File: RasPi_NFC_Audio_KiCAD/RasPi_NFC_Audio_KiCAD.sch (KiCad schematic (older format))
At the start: 19 parts, among them J1 Barrel_Jack_Switch, J2 Conn_02x20_Odd_Even, J3 Connector_01x10, U1 MIC5225-3.3V

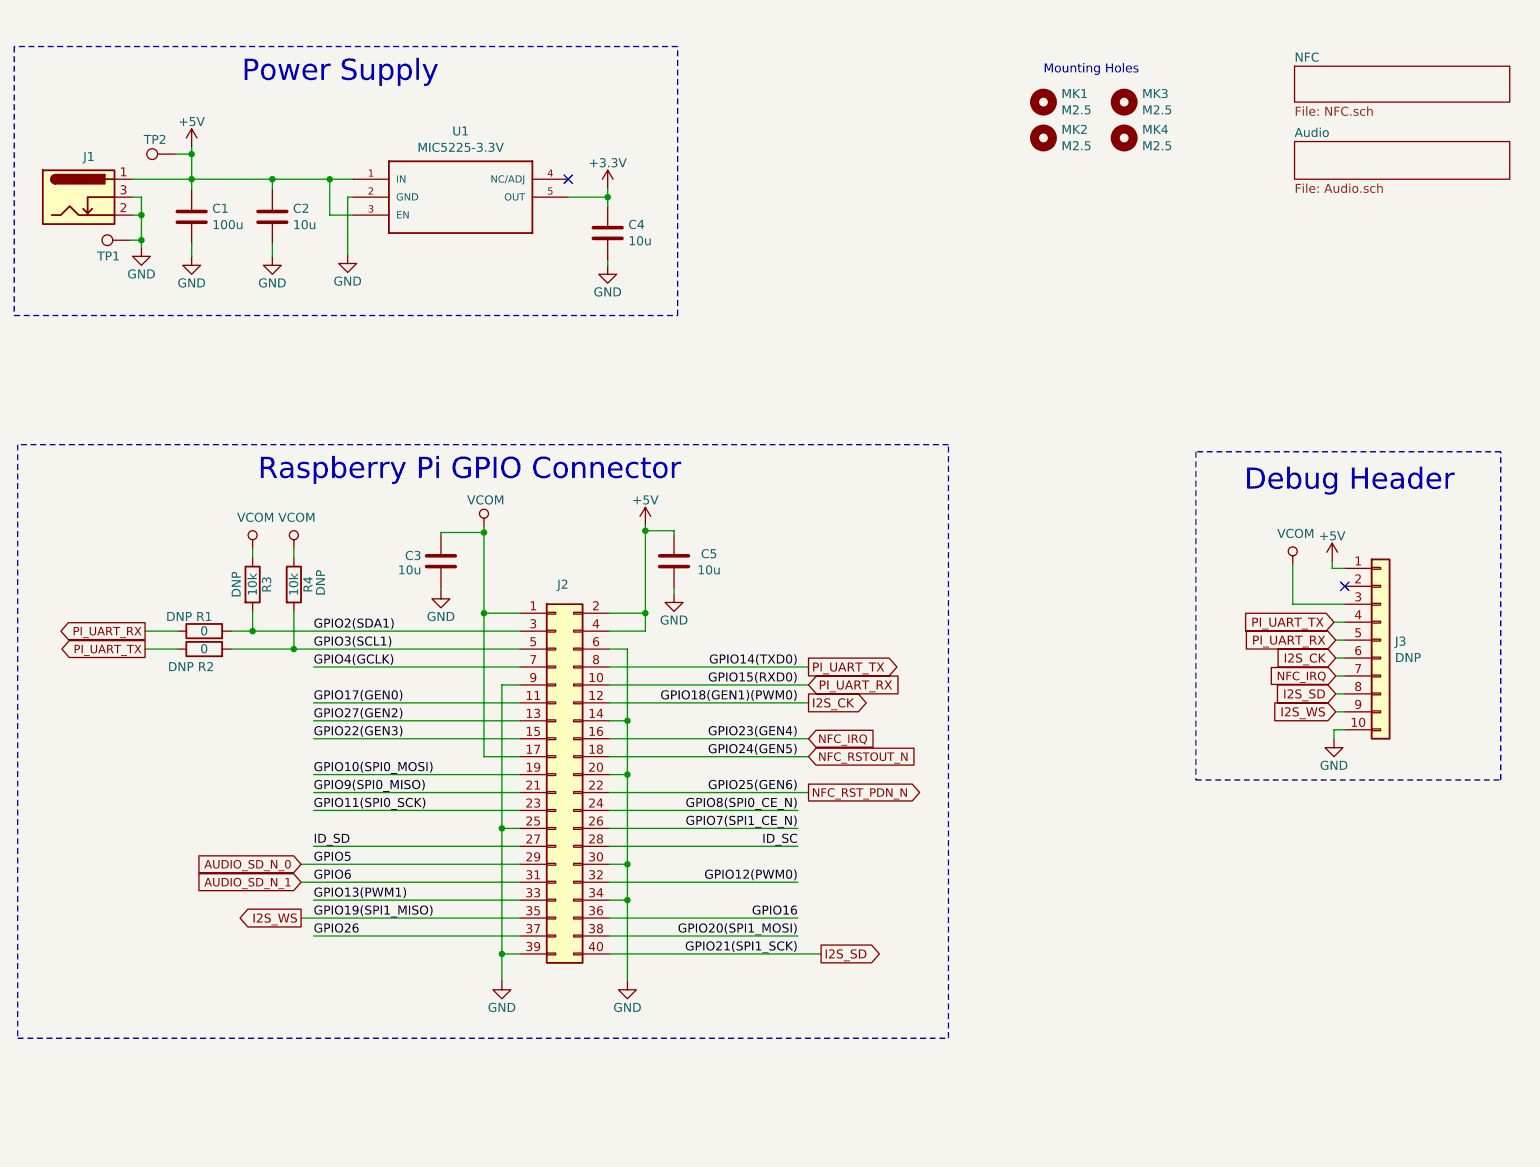
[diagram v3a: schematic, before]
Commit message: Schematic updates
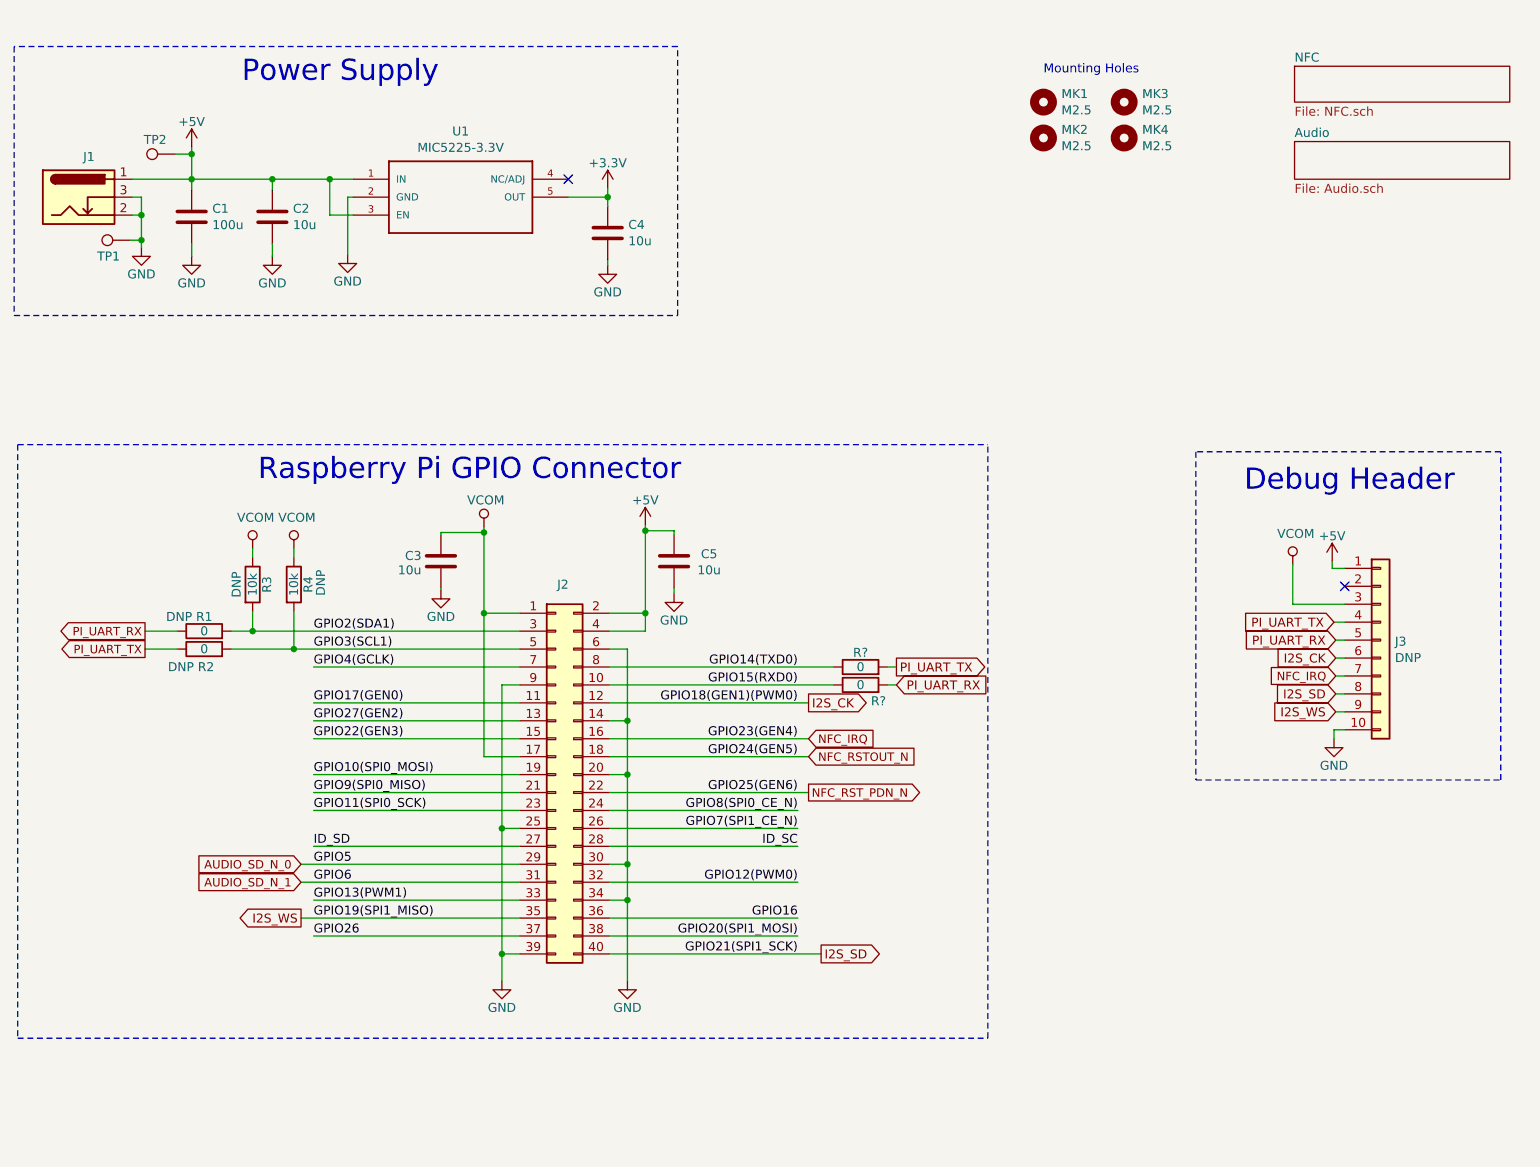
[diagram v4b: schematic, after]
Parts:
- added R? (x2): 0, Resistors_SMD:R_0603_HandSoldering, symbol Device:R
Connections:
- net PI_UART_RX: now also R?.2; no longer J2.10 (Pin_10)
- net PI_UART_TX: now also R?.2; no longer J2.8 (Pin_8)
- new net GPIO14(TXD0): J2.8 (Pin_8), R?.1
- new net GPIO15(RXD0): J2.10 (Pin_10), R?.1
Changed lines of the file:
@@
 EESchema Schematic File Version 4
 LIBS:RasPi_NFC_Audio_KiCAD-cache
-EELAYER 29 0
+EELAYER 30 0
 EELAYER END
 $Descr A4 11693 8268
@@
 Text GLabel 2670 6190 0    50   Output ~ 0
 I2S_WS
-Text GLabel 5500 4790 2    50   Output ~ 0
+Text GLabel 5990 4790 2    50   Output ~ 0
 PI_UART_TX
-Text GLabel 5500 4890 2    50   Input ~ 0
+Text GLabel 5990 4890 2    50   Input ~ 0
 PI_UART_RX
 Wire Wire Line
-	4390 4890 5500 4890
-Wire Wire Line
-	4390 4790 5500 4790
+	4390 4890 5640 4890
+Wire Wire Line
+	4390 4790 5640 4790
 $Comp
 L power:GND #PWR0101
@@
 	1090 3550 1090 6860
 Wire Notes Line
-	1090 6860 6280 6860
-Wire Notes Line
-	6280 6860 6280 3550
-Wire Notes Line
-	6280 3550 1090 3550
+	6500 6860 6500 3550
 Text Notes 2430 3760 0    118  ~ 0
 Raspberry Pi GPIO Connector
@@
 Wire Wire Line
 	1730 2170 1780 2170
+$Comp
+L Device:R R?
+U 1 1 5E234EC3
+P 5790 4790
+AR Path="/5E17696B/5E234EC3" Ref="R?"  Part="1"
+AR Path="/5E234EC3" Ref="R?"  Part="1"
+F 0 "R?" V 5870 4790 50  0000 C CNN
+F 1 "0" V 5790 4790 50  0000 C CNN
+F 2 "Resistors_SMD:R_0603_HandSoldering" V 5720 4790 50  0001 C CNN
+F 3 "" H 5790 4790 50  0001 C CNN
+F 4 "RC0603JR-070RL" H 5790 4790 50  0001 C CNN "Part #"
+F 5 "311-0.0GRCT-ND" H 5790 4790 50  0001 C CNN "DigiKey"
+	1    5790 4790
+	0    -1   -1   0
+$EndComp
+$Comp
+L Device:R R?
+U 1 1 5E23DE1B
+P 5790 4890
+AR Path="/5E17696B/5E23DE1B" Ref="R?"  Part="1"
+AR Path="/5E23DE1B" Ref="R?"  Part="1"
+F 0 "R?" V 5700 4790 50  0000 C CNN
+F 1 "0" V 5790 4890 50  0000 C CNN
+F 2 "Resistors_SMD:R_0603_HandSoldering" V 5720 4890 50  0001 C CNN
+F 3 "" H 5790 4890 50  0001 C CNN
+F 4 "RC0603JR-070RL" H 5790 4890 50  0001 C CNN "Part #"
+F 5 "311-0.0GRCT-ND" H 5790 4890 50  0001 C CNN "DigiKey"
+	1    5790 4890
+	0    -1   -1   0
+$EndComp
+Wire Wire Line
+	5940 4790 5990 4790
+Wire Wire Line
+	5940 4890 5990 4890
+Wire Notes Line
+	1090 3550 6500 3550
+Wire Notes Line
+	1090 6860 6500 6860
 $EndSCHEMATC

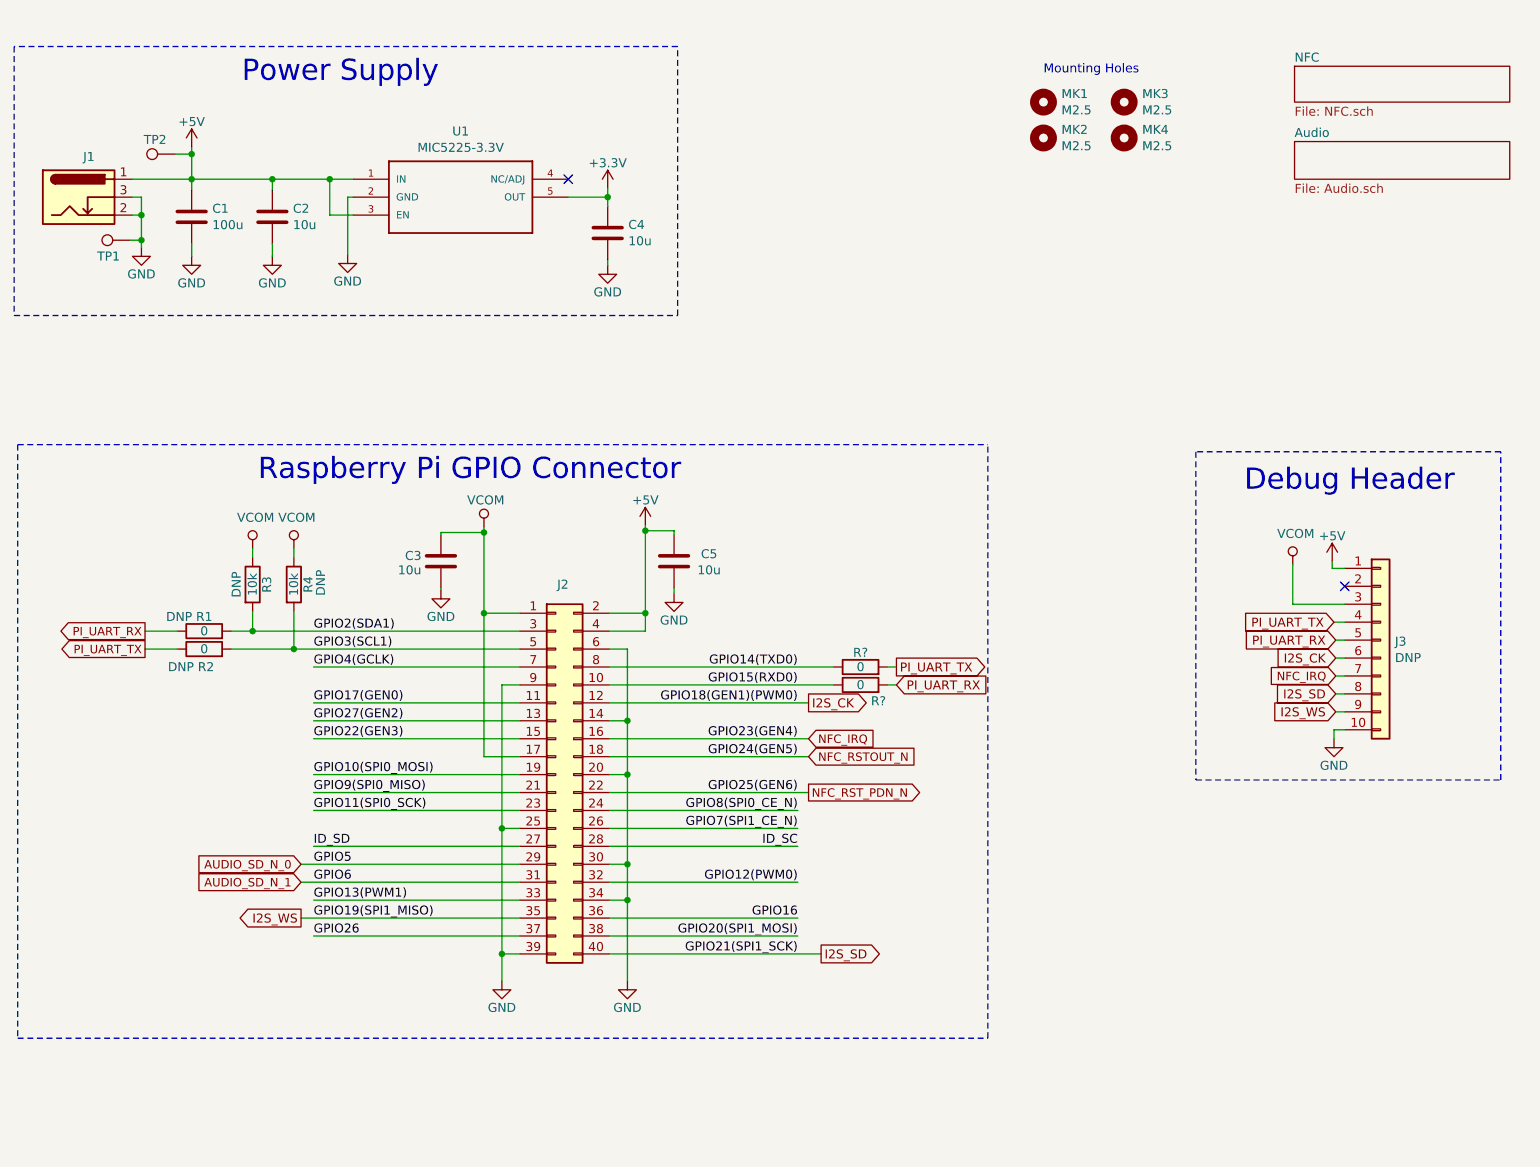
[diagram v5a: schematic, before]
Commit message: Startednfootprint assignment
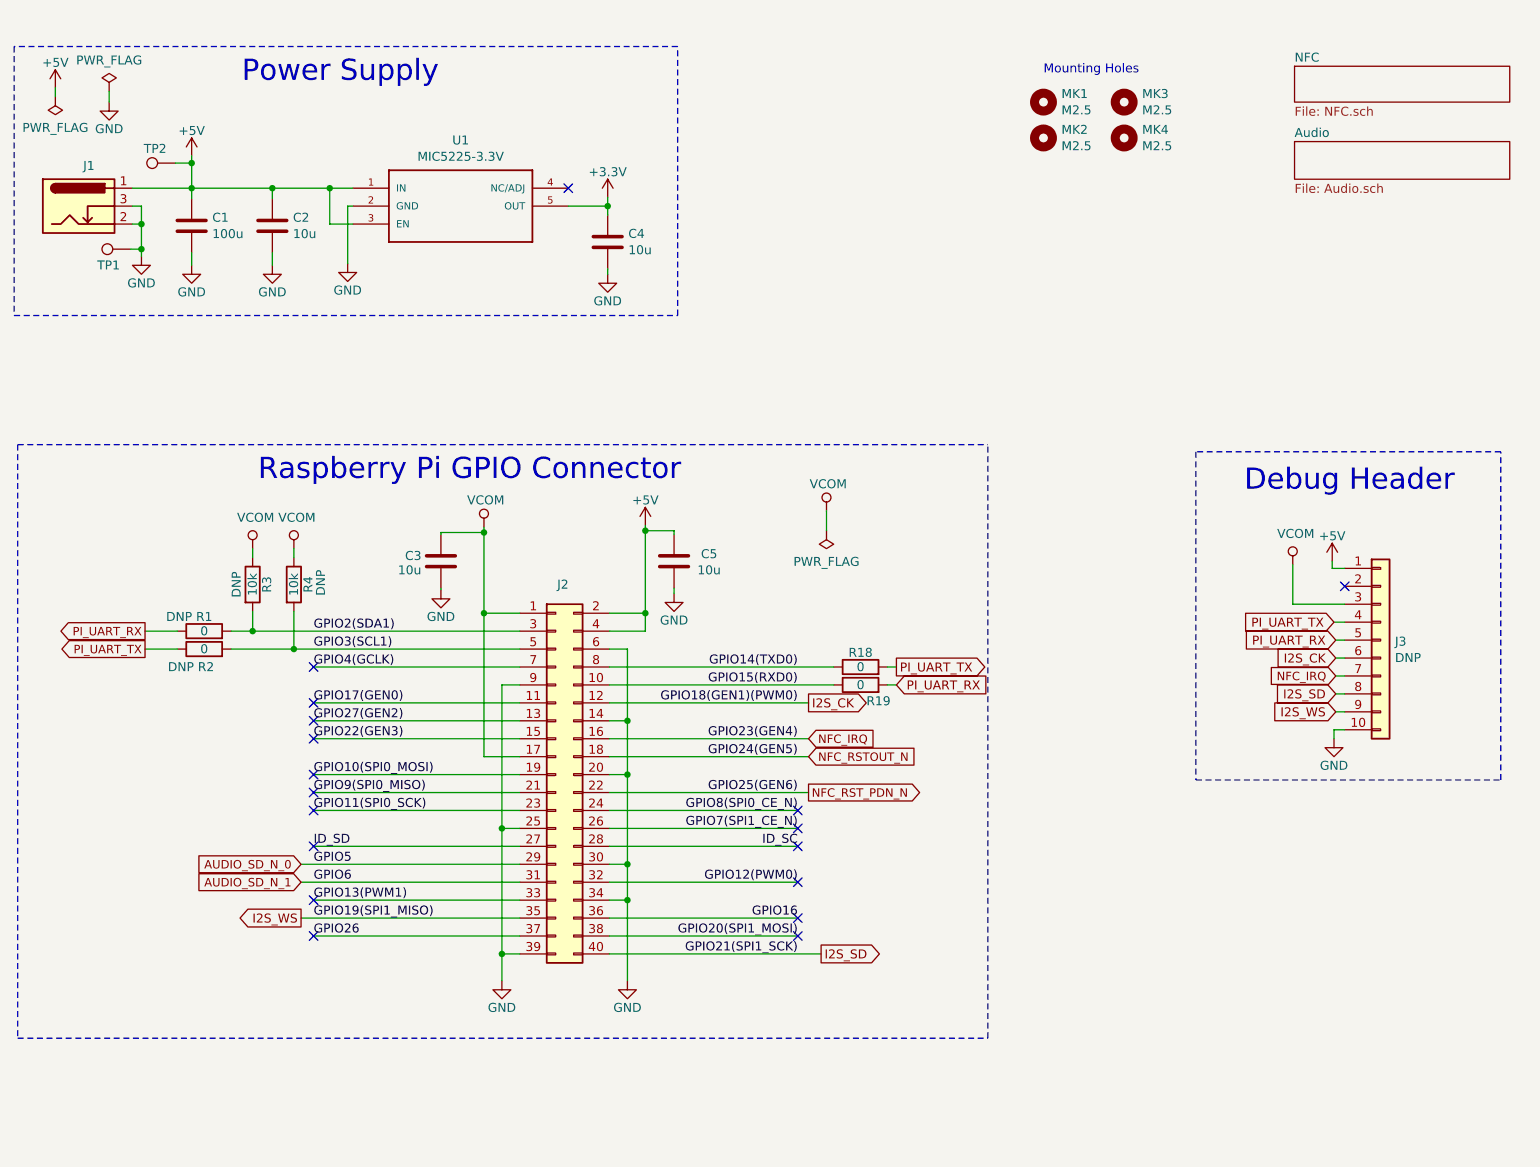
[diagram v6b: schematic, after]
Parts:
- C1: footprint (none) -> Capacitor_SMD:C_1206_3216Metric_Pad1.42x1.75mm_HandSolder
- C2, C3, C4, C5: footprint (none) -> Capacitor_SMD:C_0603_1608Metric_Pad1.05x0.95mm_HandSolder
- R1, R2, R3, R4: footprint Resistors_SMD:R_0603_HandSoldering -> Resistor_SMD:R_0603_1608Metric_Pad1.05x0.95mm_HandSolder
- R18, R19: renamed from R?; footprint Resistors_SMD:R_0603_HandSoldering -> Resistor_SMD:R_0603_1608Metric_Pad1.05x0.95mm_HandSolder
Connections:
- no-connect marks 2 -> 18
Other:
- moved on the sheet: C1, C2, C4, J1, TP1, TP2, U1

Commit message: Layout started
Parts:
- J1: footprint (none) -> Connector_BarrelJack:BarrelJack_CUI_PJ-102AH_Horizontal
- J3: footprint (none) -> Connector_PinHeader_2.54mm:PinHeader_1x10_P2.54mm_Vertical
- TP1, TP2: footprint (none) -> TestPoint:TestPoint_Keystone_5019_Minature
- U1: footprint SOT95P280X130-5N -> Package_TO_SOT_SMD:SOT-23-5
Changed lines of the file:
@@
 F 0 "U1" H 3560 2387 50  0000 C CNN
 F 1 "MIC5225-3.3V" H 3560 2296 50  0000 C CNN
-F 2 "SOT95P280X130-5N" H 2960 2120 50  0001 L BNN
+F 2 "Package_TO_SOT_SMD:SOT-23-5" H 2960 2120 50  0001 L BNN
 F 3 "" H 2960 2120 50  0001 L BNN
 F 4 "SOT-23-5 Microchip" H 2960 2120 50  0001 L BNN "Field4"
@@
 F 0 "J3" H 8770 4632 50  0000 L CNN
 F 1 "Connector_01x10" H 8770 4586 50  0001 L CNN
-F 2 "" H 8690 4640 50  0001 C CNN
+F 2 "Connector_PinHeader_2.54mm:PinHeader_1x10_P2.54mm_Vertical" H 8690 4640 50  0001 C CNN
 F 3 "~" H 8690 4640 50  0001 C CNN
 F 4 "M20-9991046" H 8690 4640 50  0001 C CNN "Part #"
@@
 F 0 "TP2" V 2050 2030 50  0000 L CNN
 F 1 "TestPoint" H 2028 2007 50  0001 L CNN
-F 2 "" H 2170 1980 50  0001 C CNN
+F 2 "TestPoint:TestPoint_Keystone_5019_Minature" H 2170 1980 50  0001 C CNN
 F 3 "~" H 2170 1980 50  0001 C CNN
 	1    1970 1980
@@
 F 0 "TP1" V 1630 2520 50  0000 L CNN
 F 1 "TestPoint" H 1778 2487 50  0001 L CNN
-F 2 "" H 1920 2460 50  0001 C CNN
+F 2 "TestPoint:TestPoint_Keystone_5019_Minature" H 1920 2460 50  0001 C CNN
 F 3 "~" H 1920 2460 50  0001 C CNN
 	1    1720 2460
@@
 F 0 "J1" H 1487 2445 50  0000 C CNN
 F 1 "Barrel_Jack_Switch" H 1487 2446 50  0001 C CNN
-F 2 "" H 1480 2180 50  0001 C CNN
+F 2 "Connector_BarrelJack:BarrelJack_CUI_PJ-102AH_Horizontal" H 1480 2180 50  0001 C CNN
 F 3 "~" H 1480 2180 50  0001 C CNN
 F 4 "PJ-102AH" H 1430 2220 50  0001 C CNN "Part #"
